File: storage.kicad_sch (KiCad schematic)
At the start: 6 parts, among them J14 DM3CS-SF, U7 MX25V4006EM1I-13G

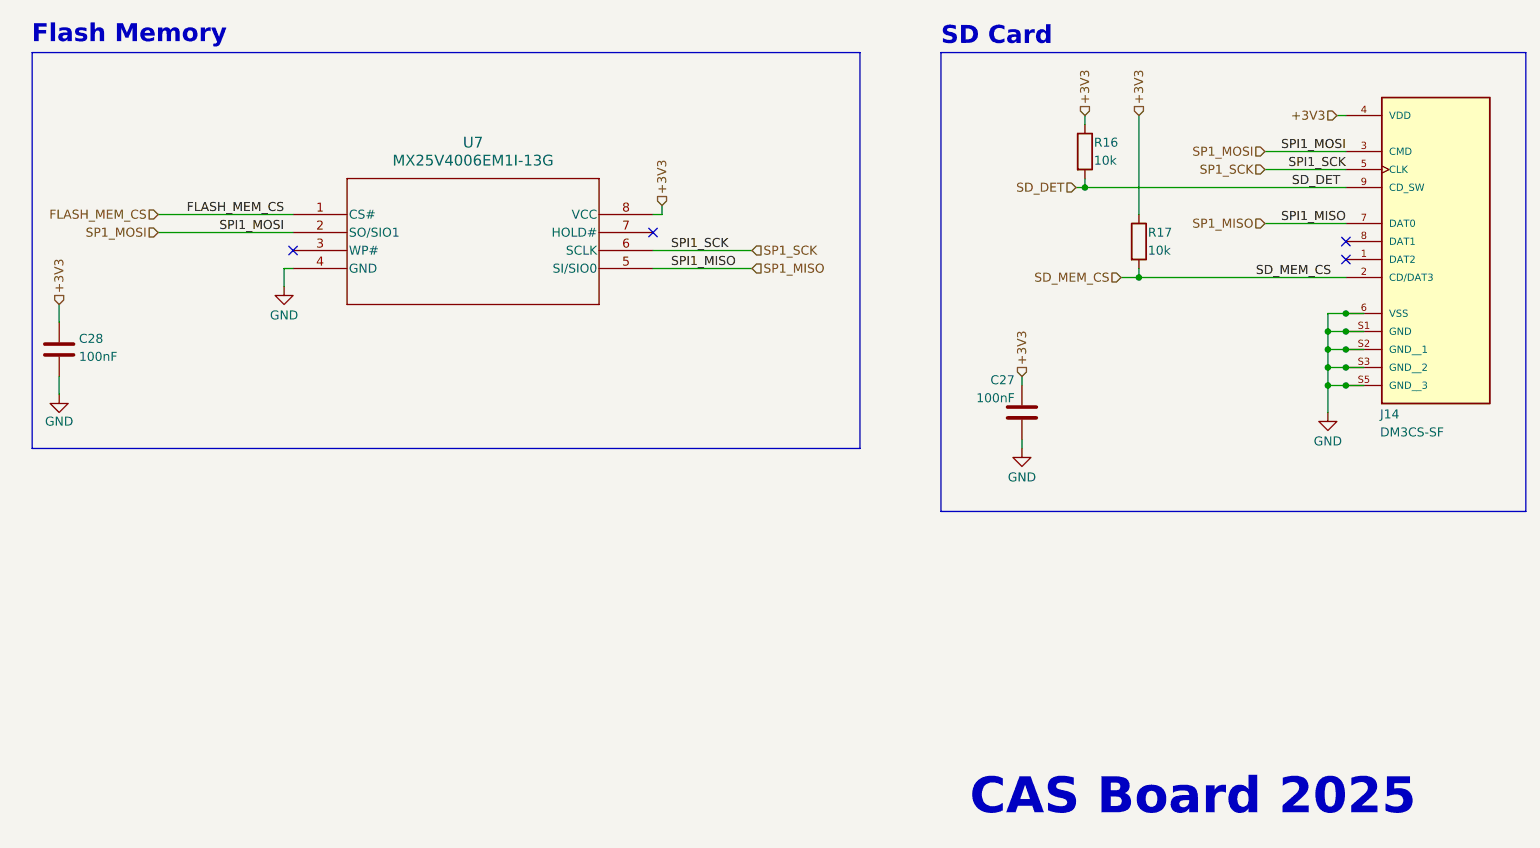
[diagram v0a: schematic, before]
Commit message: Revised to improve buck converters and free up space on board
Fixed overvoltage error on encoder (5v -> 3v)
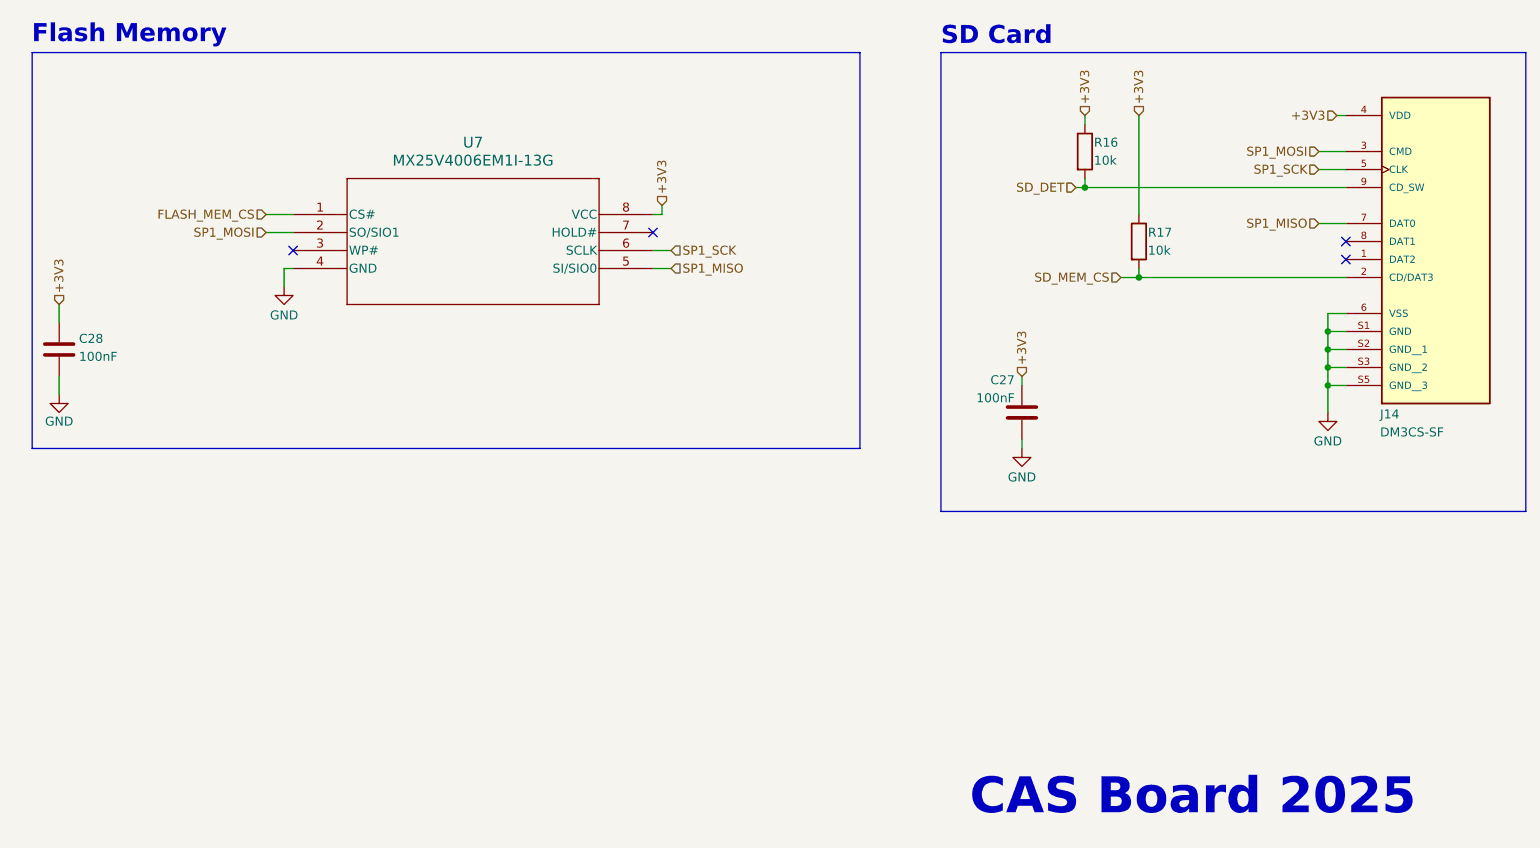
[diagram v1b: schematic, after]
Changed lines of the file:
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@@
 	)
 	(junction
-		(at 231.14 107.95)
-		(diameter 0)
-		(color 0 0 0 0)
-	)
-	(junction
 		(at 194.31 87.63)
 		(diameter 0)
@@
 	)
 	(junction
-		(at 231.14 105.41)
-		(diameter 0)
-		(color 0 0 0 0)
-	)
-	(junction
 		(at 201.93 100.33)
 		(diameter 0)
@@
 	)
 	(junction
-		(at 231.14 113.03)
-		(diameter 0)
-		(color 0 0 0 0)
-	)
-	(junction
 		(at 228.6 113.03)
 		(diameter 0)
@@
 	)
 	(junction
-		(at 231.14 115.57)
-		(diameter 0)
-		(color 0 0 0 0)
-	)
-	(junction
 		(at 228.6 110.49)
 		(diameter 0)
 		(color 0 0 0 0)
 	)
-	(junction
-		(at 231.14 110.49)
-		(diameter 0)
-		(color 0 0 0 0)
-	)
 	(no_connect
 		(at 231.14 95.25)
@@
 	(wire
 		(pts
-			(xy 233.68 113.03) (xy 231.14 113.03)
-		)
-		(stroke
-			(width 0)
-			(type default)
-		)
-	)
-	(wire
-		(pts
 			(xy 231.14 107.95) (xy 228.6 107.95)
 		)
@@
 	(wire
 		(pts
-			(xy 233.68 107.95) (xy 231.14 107.95)
-		)
-		(stroke
-			(width 0)
-			(type default)
-		)
-	)
-	(wire
-		(pts
 			(xy 49.53 114.3) (xy 49.53 116.84)
 		)
@@
 		)
 	)
-	(wire
-		(pts
-			(xy 233.68 115.57) (xy 231.14 115.57)
-		)
-		(stroke
-			(width 0)
-			(type default)
-		)
-	)
 	(polyline
 		(pts
@@
 	(wire
 		(pts
-			(xy 219.71 82.55) (xy 231.14 82.55)
+			(xy 227.33 82.55) (xy 231.14 82.55)
 		)
 		(stroke
@@
 	(wire
 		(pts
-			(xy 63.5 91.44) (xy 82.55 91.44)
+			(xy 78.74 91.44) (xy 82.55 91.44)
 		)
 		(stroke
@@
 		)
 	)
-	(wire
-		(pts
-			(xy 233.68 110.49) (xy 231.14 110.49)
-		)
-		(stroke
-			(width 0)
-			(type default)
-		)
-	)
 	(polyline
 		(pts
@@
 	(wire
 		(pts
-			(xy 233.68 105.41) (xy 231.14 105.41)
-		)
-		(stroke
-			(width 0)
-			(type default)
-		)
-	)
-	(wire
-		(pts
 			(xy 49.53 104.14) (xy 49.53 106.68)
 		)
@@
 	(wire
 		(pts
-			(xy 63.5 93.98) (xy 82.55 93.98)
+			(xy 78.74 93.98) (xy 82.55 93.98)
 		)
 		(stroke
@@
 	(wire
 		(pts
-			(xy 219.71 85.09) (xy 231.14 85.09)
+			(xy 227.33 85.09) (xy 231.14 85.09)
 		)
 		(stroke
@@
 	(wire
 		(pts
-			(xy 219.71 92.71) (xy 231.14 92.71)
+			(xy 227.33 92.71) (xy 231.14 92.71)
 		)
 		(stroke
@@
 	(wire
 		(pts
-			(xy 133.35 99.06) (xy 147.32 99.06)
+			(xy 133.35 99.06) (xy 135.89 99.06)
 		)
 		(stroke
@@
 	(wire
 		(pts
-			(xy 133.35 96.52) (xy 147.32 96.52)
+			(xy 133.35 96.52) (xy 135.89 96.52)
 		)
 		(stroke
@@
 		)
 	)
-	(label "SPI1_SCK"
-		(at 135.89 96.52 0)
-		(effects
-			(font
-				(size 1.27 1.27)
-			)
-			(justify left bottom)
-		)
-	)
-	(label "SPI1_SCK"
-		(at 231.14 85.09 180)
-		(effects
-			(font
-				(size 1.27 1.27)
-			)
-			(justify right bottom)
-		)
-	)
-	(label "FLASH_MEM_CS"
-		(at 81.28 91.44 180)
-		(effects
-			(font
-				(size 1.27 1.27)
-			)
-			(justify right bottom)
-		)
-	)
-	(label "SD_DET"
-		(at 223.52 87.63 0)
-		(effects
-			(font
-				(size 1.27 1.27)
-			)
-			(justify left bottom)
-		)
-	)
-	(label "SPI1_MISO"
-		(at 135.89 99.06 0)
-		(effects
-			(font
-				(size 1.27 1.27)
-			)
-			(justify left bottom)
-		)
-	)
-	(label "SPI1_MOSI"
-		(at 231.14 82.55 180)
-		(effects
-			(font
-				(size 1.27 1.27)
-			)
-			(justify right bottom)
-		)
-	)
-	(label "SD_MEM_CS"
-		(at 218.44 100.33 0)
-		(effects
-			(font
-				(size 1.27 1.27)
-			)
-			(justify left bottom)
-		)
-	)
-	(label "SPI1_MISO"
-		(at 231.14 92.71 180)
-		(effects
-			(font
-				(size 1.27 1.27)
-			)
-			(justify right bottom)
-		)
-	)
-	(label "SPI1_MOSI"
-		(at 81.28 93.98 180)
-		(effects
-			(font
-				(size 1.27 1.27)
-			)
-			(justify right bottom)
-		)
-	)
 	(hierarchical_label "+3V3"
 		(shape input)
@@
 	(hierarchical_label "SP1_SCK"
 		(shape input)
-		(at 147.32 96.52 0)
+		(at 135.89 96.52 0)
 		(effects
 			(font
@@
 	(hierarchical_label "SP1_MOSI"
 		(shape input)
-		(at 219.71 82.55 180)
+		(at 227.33 82.55 180)
 		(effects
 			(font
@@
 	(hierarchical_label "SP1_SCK"
 		(shape input)
-		(at 219.71 85.09 180)
+		(at 227.33 85.09 180)
 		(effects
 			(font
@@
 	(hierarchical_label "FLASH_MEM_CS"
 		(shape input)
-		(at 63.5 91.44 180)
+		(at 78.74 91.44 180)
 		(effects
 			(font
@@
 	(hierarchical_label "SP1_MOSI"
 		(shape input)
-		(at 63.5 93.98 180)
+		(at 78.74 93.98 180)
 		(effects
 			(font
@@
 	(hierarchical_label "SP1_MISO"
 		(shape input)
-		(at 219.71 92.71 180)
+		(at 227.33 92.71 180)
 		(effects
 			(font
@@
 	(hierarchical_label "SP1_MISO"
 		(shape input)
-		(at 147.32 99.06 0)
+		(at 135.89 99.06 0)
 		(effects
 			(font
